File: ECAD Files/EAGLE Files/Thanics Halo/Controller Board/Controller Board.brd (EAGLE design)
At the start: 95.6 x 57.3 mm, 154 parts, among them J10 EDGE_CONNECTOR_20POS, J2 3.5_TOUCHSCREEN, J3 USB_MICRO_B_SMT, J5 EDGE_CONNECTOR_20POS, J6 POWER_CONNECTOR, J7 HDMI, J8 2_PIN_CONNECTOR, J9 USB_A_RECEPT, Q2 2N7002P_MOSFET, U1 AAT3620_BATT_CHARGER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

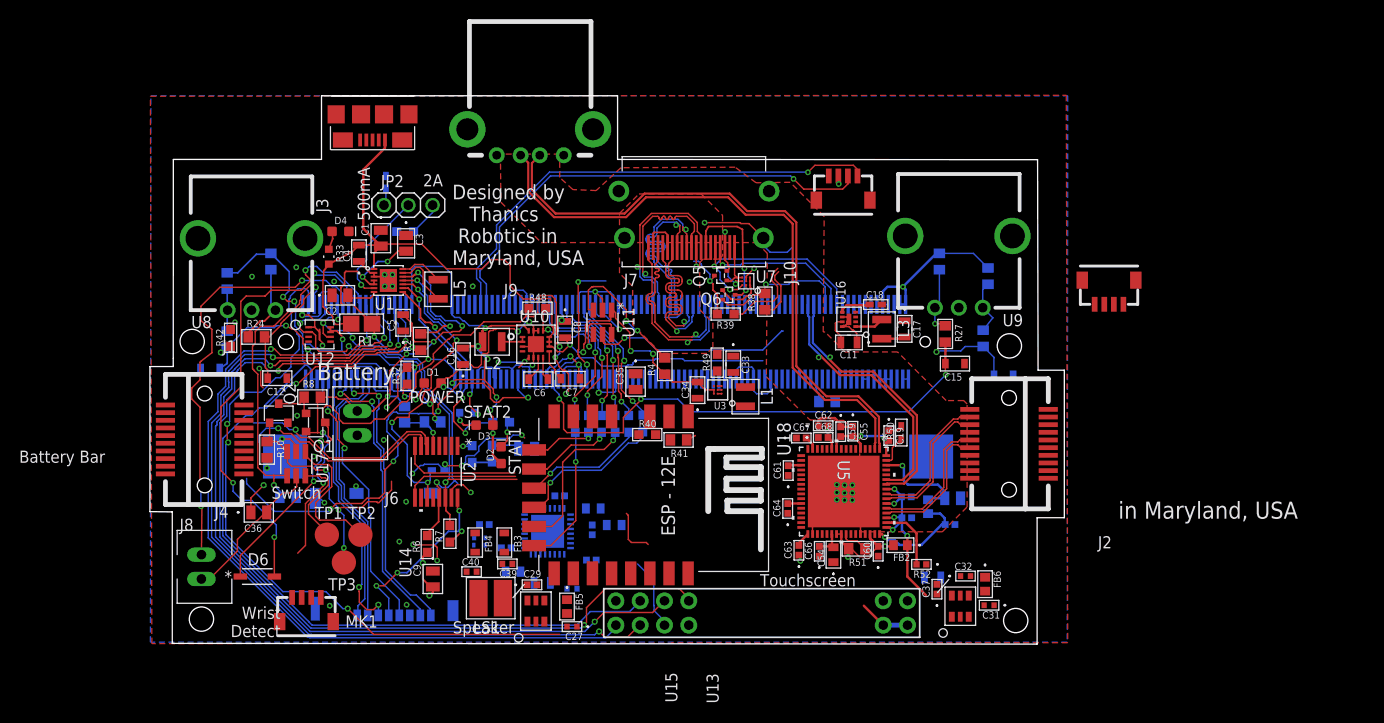
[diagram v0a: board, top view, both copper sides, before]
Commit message: Reorganized ECAD Files
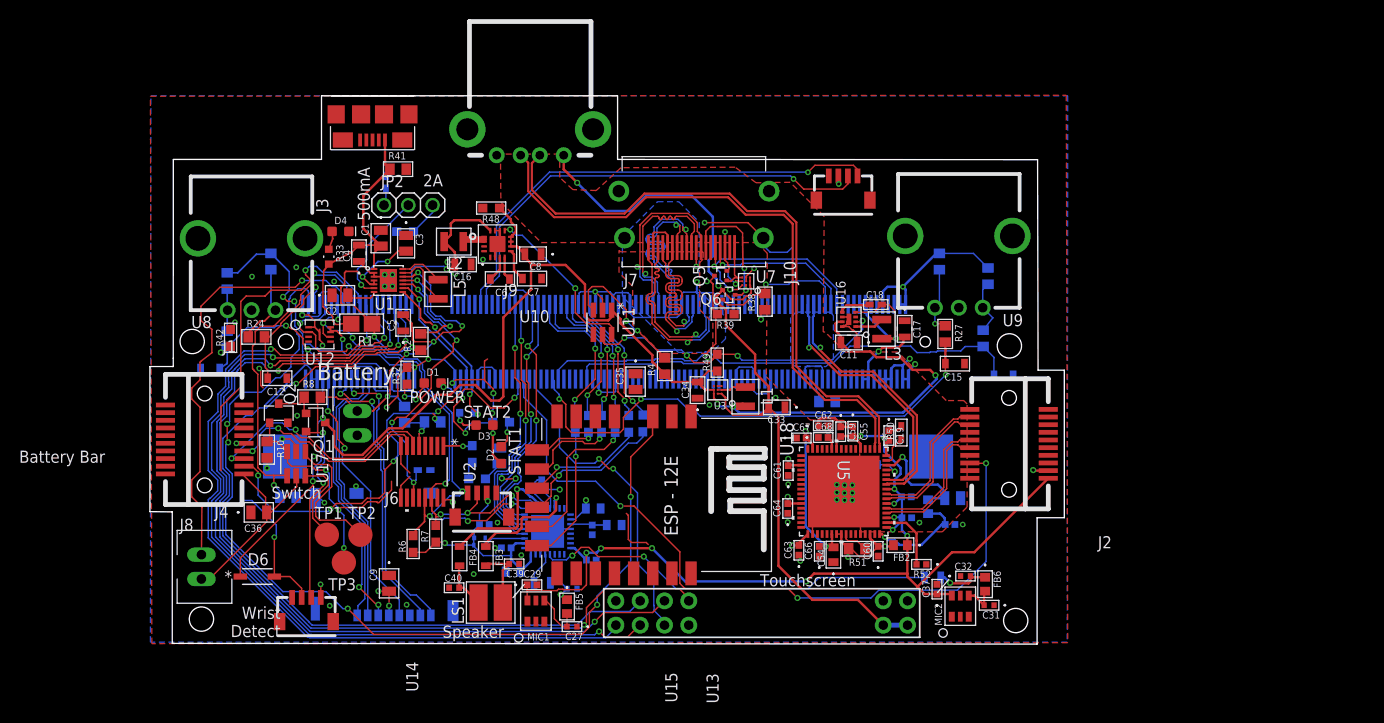
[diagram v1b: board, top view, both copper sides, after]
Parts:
- moved J11 68.4 mm to (36.6, 16.0), turned to 180 degrees
- moved R41 40.7 mm to (27.8, 49.8), turned to 0 degrees
- moved R40 23.3 mm to (76.9, 18.9), flipped to the bottom
- moved R48 11.5 mm to (37.5, 45.7), turned to 180 degrees
- moved C7 11.2 mm to (41.8, 38.4)
- moved U10 11.2 mm to (38.2, 42.0)
- moved C6 11.2 mm to (38.5, 38.3)
- moved L2 11.2 mm to (33.6, 42.2)
- moved C16 9.60 mm to (34.6, 39.8), turned to 180 degrees
- moved C8 8.56 mm to (41.9, 40.9), turned to 180 degrees
- moved C33 6.39 mm to (67.4, 24.9), turned to 180 degrees
- moved C9 4.59 mm to (26.9, 6.50)
- moved R13 3.08 mm to (36.1, 17.4), turned to 180 degrees
- moved C10 2.95 mm to (38.4, 19.8), turned to 90 degrees
- moved C40 2.48 mm to (33.7, 6.05)
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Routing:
- net +5V: track 11.2 -> 92.8 mm, vias 0 -> 2
- net J2_SW: track 0.00 -> 77.5 mm, vias 0 -> 3
- net 3.3V_A: track 30.1 -> 107.5 mm, vias 7 -> 11
- net GND: track 228.9 -> 176.9 mm, vias 61 -> 51
- net BATT_OUTPUT: track 93.3 -> 144.0 mm, vias 6 -> 5
- net LIN1: track 0.00 -> 42.4 mm, vias 0 -> 2
- net I2S_LRCLK: track 0.00 -> 35.3 mm, vias 0 -> 4
- net USB_5V: track 65.7 -> 30.9 mm, vias 3 -> 0
- net ID_SD: track 73.1 -> 101.8 mm, vias 3 -> 5
- net I2S_CLK: track 0.00 -> 27.7 mm, vias 0 -> 2
- net I2S_DAC: track 0.00 -> 26.5 mm, vias 0 -> 2
- net I2S_ADC: track 0.00 -> 25.7 mm, vias 0 -> 2
- net IRQ: track 8.65 -> 33.7 mm, vias 0 -> 2
- net +3V3: track 187.5 -> 207.5 mm, vias 24 -> 33
- net ENCODER2_B: track 32.4 -> 51.7 mm, vias 1 -> 0
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- added copper zone on layer 16, net N$52
- added copper zone on layer 16, net N$63
- added copper zone on layer 2, net N$64
- added copper zone on layer 15, net N$65
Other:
- board text removed: "MK1"
- board text removed: "in Maryland, USA"
